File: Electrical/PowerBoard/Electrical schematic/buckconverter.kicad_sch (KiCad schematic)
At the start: 6 parts, among them U1 LMZ22005TZ/NOPB

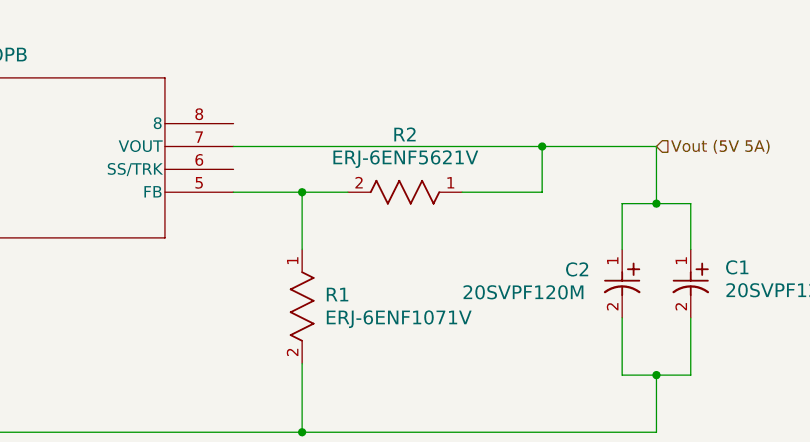
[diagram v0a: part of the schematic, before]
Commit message: finishing pcb
adding mounting holes and different resistor for buck converter to convert to 5.15V.
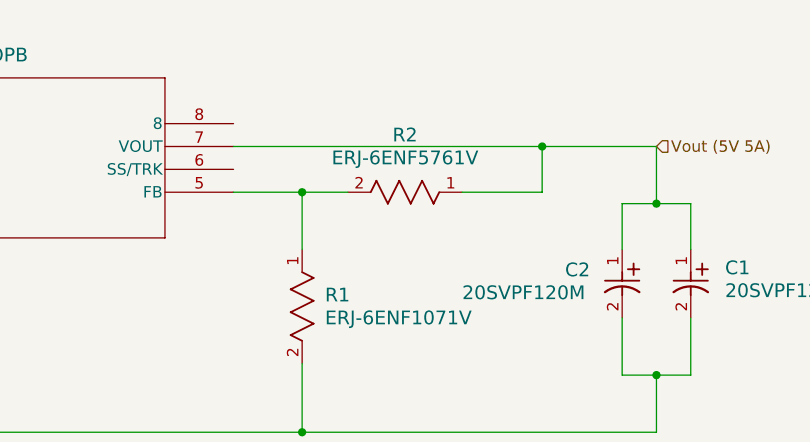
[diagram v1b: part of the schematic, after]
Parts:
- removed R2: ERJ-6ENF5621V, RC0805N_PAN, symbol 5.62kOhm Resistor:ERJ-6ENF5621V
- added R2: ERJ-6ENF5761V, RC0805N_PAN, symbol 2025-02-23_03-04-54:ERJ-6ENF5761V
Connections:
- net Vout (5V 5A): now also R2.1
- net at R1.1, U1.5 (FB): now also R2.2
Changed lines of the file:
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@@
 	)
 	(symbol
-		(lib_id "5.62kOhm Resistor:ERJ-6ENF5621V")
+		(lib_id "2025-02-23_03-04-54:ERJ-6ENF5761V")
 		(at 187.96 66.04 0)
 		(unit 1)
@@
 			)
 		)
-		(property "Value" "ERJ-6ENF5621V"
+		(property "Value" "ERJ-6ENF5761V"
 			(at 194.31 62.23 0)
 			(effects
@@
 			)
 		)
-		(property "Datasheet" "ERJ-6ENF5621V"
+		(property "Datasheet" "ERJ-6ENF5761V"
 			(at 187.96 66.04 0)
 			(effects
@@
 			)
 		)
+		(pin "2"
+		)
 		(pin "1"
 		)
-		(pin "2"
-		)
 		(instances

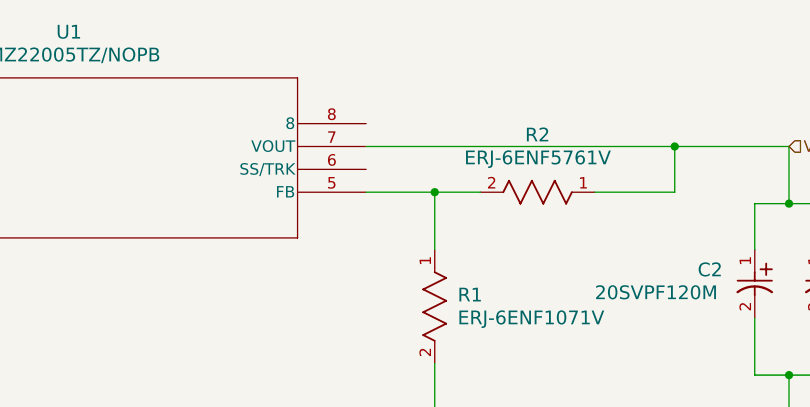
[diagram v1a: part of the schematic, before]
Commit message: Buck Board Version 1
Added capacitor for Pi rail
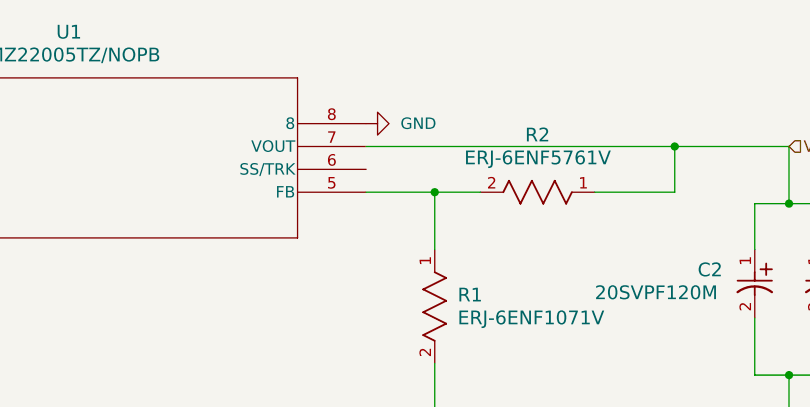
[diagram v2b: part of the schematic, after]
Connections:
- net GND: now also U1.8
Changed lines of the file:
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@@
+	)
+	(symbol
+		(lib_id "power:GND")
+		(at 175.26 58.42 90)
+		(unit 1)
+		(exclude_from_sim no)
+		(in_bom yes)
+		(on_board yes)
+		(dnp no)
+		(fields_autoplaced yes)
+		(property "Reference" "#PWR011"
+			(at 181.61 58.42 0)
+			(effects
+				(font
+					(size 1.27 1.27)
+				)
+				(hide yes)
+			)
+		)
+		(property "Value" "GND"
+			(at 179.07 58.4199 90)
+			(effects
+				(font
+					(size 1.27 1.27)
+				)
+				(justify right)
+			)
+		)
+		(property "Footprint" ""
+			(at 175.26 58.42 0)
+			(effects
+				(font
+					(size 1.27 1.27)
+				)
+				(hide yes)
+			)
+		)
+		(property "Datasheet" ""
+			(at 175.26 58.42 0)
+			(effects
+				(font
+					(size 1.27 1.27)
+				)
+				(hide yes)
+			)
+		)
+		(property "Description" "Power symbol creates a global label with name \"GND\" , ground"
+			(at 175.26 58.42 0)
+			(effects
+				(font
+					(size 1.27 1.27)
+				)
+				(hide yes)
+			)
+		)
+		(pin "1"
+		)
+		(instances
+			(project ""
+				(path "/f95f296f-a4bf-4952-bdc7-66087a6cc347/c3262f5d-4eb7-401f-8382-bbb2aadd6328"
+					(reference "#PWR011")
+					(unit 1)
+				)
+			)
+		)
 	)
 	(symbol
